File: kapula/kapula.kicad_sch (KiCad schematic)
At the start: 153 parts, among them J1 Conn_02x10_Odd_Even, J12 U.FL, J13 U.FL, J3 Conn_02x10_Odd_Even, J4 Conn_ARM_JTAG_SWD_10, J5 U.FL, J9 U.FL, Q1 AO3401A, Q1 BSS84, Q2 AO3401A, Q3 AO3400A, Q5 AO3400A, Q6 AO3400A, T1 BW21S7511A01TF, T2 BW21S7511A01TF, T3 BW21S7511A01TF, T4 BW21S7511A01TF, U1 XC6206P332MR, U2 TP4054, U3 DW01+G, U5 EFR32FG14P233F256GM48-B, U6 XA213-G4J, X1 DSB221SDN, Y1 32768 Hz

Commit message: PCB: Route TX lowpass again
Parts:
- C24: footprint Capacitor_SMD:C_0402_1005Metric -> kapula:C_0402_to_0603_HandSolder
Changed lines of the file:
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@@
       (effects (font (size 1.27 1.27)))
     )
-    (property "Footprint" "Capacitor_SMD:C_0402_1005Metric" (at 270.51 127.9652 0)
+    (property "Footprint" "kapula:C_0402_to_0603_HandSolder" (at 270.51 127.9652 0)
       (effects (font (size 1.27 1.27)) hide)
     )

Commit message: PCB: Miscellaneous routing
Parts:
- removed TP4: ~, TestPoint:TestPoint_Pad_D1.0mm, symbol Connector:TestPoint
- added C28: 220p, Capacitor_SMD:C_0402_1005Metric, symbol Device:C
- added R22: 0, kapula:R_0402_to_0603_HandSolder, symbol Device:R
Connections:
- net PB12 is gone; now on net SPK_SDN: U5.32 (PB12)
- net GND: now also C28.2
- net SPK_SDN: now also R22.1; no longer U8.1 (SHUTDOWN)
- net VOL_In: now also C28.1
- new net AMP_SDN: R22.2, U8.1 (SHUTDOWN)
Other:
- note added: "TODO: Choose pin for VBAT_ADC (maybe PA4?)"
- note removed: "TODO: Choose pins for SPK_SDN and VBAT_ADC"
- moved on the sheet: C67, C68, C69, C70, C71, FB7, FB8, R39, R40, R41, R42, U8

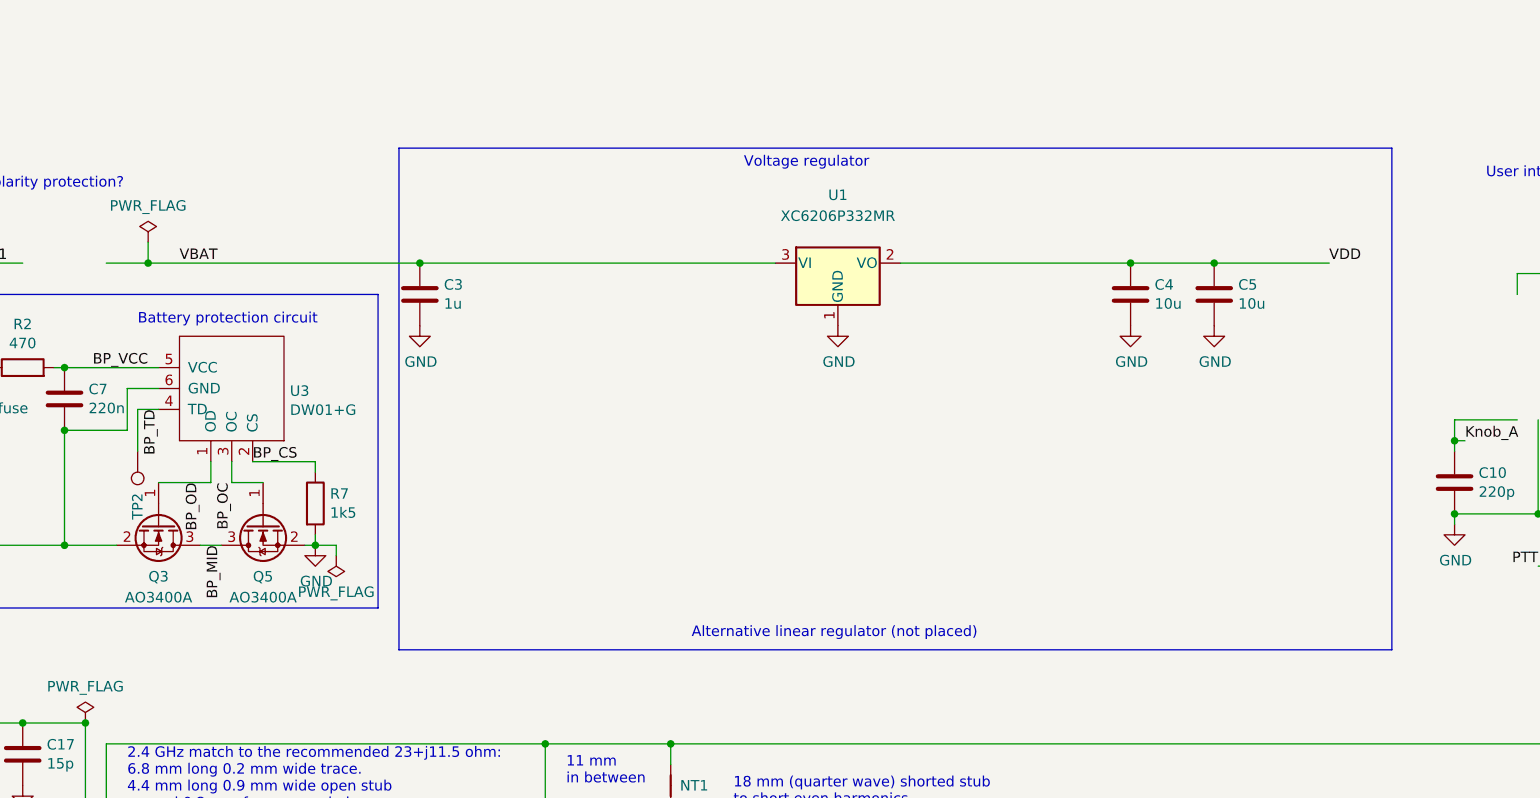
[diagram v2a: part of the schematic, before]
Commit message: PCB: Place and route battery voltage circuits
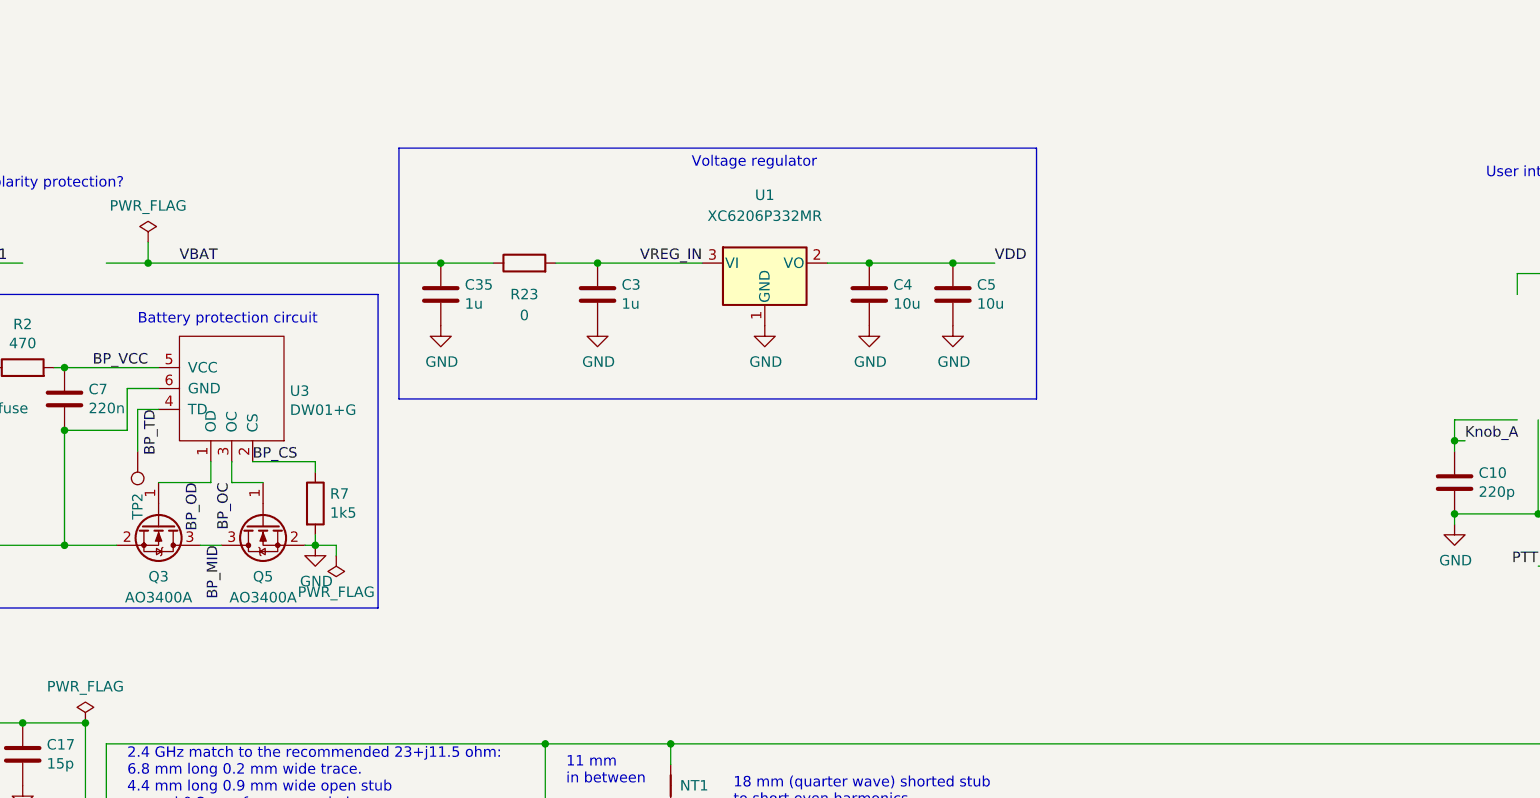
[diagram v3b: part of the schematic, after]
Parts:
- added C35: 1u, Capacitor_SMD:C_0603_1608Metric, symbol Device:C
- added R23: 0, kapula:R_0402_to_0603_HandSolder, symbol Device:R
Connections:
- net GND: now also C35.2
- net VBAT: now also C35.1, R23.1; no longer C3.1, U1.3 (VI)
- new net VREG_IN: C3.1, R23.2, U1.3 (VI)
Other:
- note removed: "Alternative linear regulator (not placed)"
- moved on the sheet: C3, C4, C5, U1

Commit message: PCB: More miscellaneous routing
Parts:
- removed TP3, TP5, TP6: ~, TestPoint:TestPoint_Pad_D1.0mm, symbol Connector:TestPoint
- FB1, FB2: footprint Inductor_SMD:L_0805_2012Metric_Pad1.05x1.20mm_HandSolder -> Inductor_SMD:L_0603_1608Metric_Pad1.05x0.95mm_HandSolder; LCSC TBD -> C1002
- L1: footprint Inductor_SMD:L_Wuerth_MAPI-3010 -> Inductor_SMD:L_1206_3216Metric; LCSC C76865 -> C1049
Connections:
- net GND: now also J6.1 (Pin_1), J6.3 (Pin_3), J6.4 (Pin_4)
- net PA0_TX: now also J3.15 (Pin_15); no longer J6.3 (Pin_3)
- net PA1_RX: now also J3.13 (Pin_13); no longer J6.4 (Pin_4)
- net PA4: now also J3.11 (Pin_11)
- net PA5: now also J3.9 (Pin_9)
- net PB11: now also J3.7 (Pin_7)
- net RESET: no longer J6.1 (Pin_1)
- net RX_EN: now also J3.19 (Pin_19)
- net TX_EN: now also J3.17 (Pin_17)
- net VBAT: now also J3.1 (Pin_1)
- net VDD: now also J3.3 (Pin_3)
- net VDDS: now also J3.5 (Pin_5)
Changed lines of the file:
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@@
   (junction (at 95.25 99.06) (diameter 0) (color 0 0 0 0)
   )
+  (junction (at 334.01 229.87) (diameter 0) (color 0 0 0 0)
+  )
   (junction (at 80.01 255.27) (diameter 0) (color 0 0 0 0)
   )
@@
   (junction (at 69.85 231.14) (diameter 0) (color 0 0 0 0)
   )
+  (junction (at 334.01 232.41) (diameter 0) (color 0 0 0 0)
+  )
   (junction (at 340.36 48.26) (diameter 0) (color 0 0 0 0)
   )
@@
     (stroke (width 0) (type default))
   )
+  (wire (pts (xy 334.01 229.87) (xy 334.01 232.41))
+    (stroke (width 0) (type default))
+  )
   (wire (pts (xy 218.44 177.8) (xy 226.06 177.8))
     (stroke (width 0) (type default))
@@
     (stroke (width 0) (type default))
   )
-  (wire (pts (xy 135.89 93.98) (xy 135.89 101.6))
-    (stroke (width 0) (type default))
-  )
   (wire (pts (xy 173.99 177.8) (xy 185.42 177.8))
     (stroke (width 0) (type default))
@@
     (stroke (width 0) (type default))
   )
-  (wire (pts (xy 140.97 93.98) (xy 140.97 101.6))
-    (stroke (width 0) (type default))
-  )
   (wire (pts (xy 181.61 26.67) (xy 217.17 26.67))
     (stroke (width 0) (type default))
@@
     (stroke (width 0) (type default))
   )
+  (wire (pts (xy 334.01 227.33) (xy 334.01 229.87))
+    (stroke (width 0) (type default))
+  )
   (wire (pts (xy 238.76 233.68) (xy 252.73 233.68))
     (stroke (width 0) (type default))
@@
     (stroke (width 0) (type default))
   )
-  (wire (pts (xy 138.43 101.6) (xy 138.43 93.98))
-    (stroke (width 0) (type default))
-  )
   (wire (pts (xy 307.34 157.48) (xy 307.34 158.75))
     (stroke (width 0) (type default))
@@
     (stroke (width 0) (type default))
   )
+  (wire (pts (xy 334.01 232.41) (xy 334.01 234.95))
+    (stroke (width 0) (type default))
+  )
   (polyline (pts (xy 143.51 215.9) (xy 298.45 215.9))
     (stroke (width 0) (type default))
@@
     (effects (font (size 1.27 1.27)) (justify right bottom))
   )
-  (label "PA1_RX" (at 334.01 234.95 0) (fields_autoplaced)
+  (label "PA1_RX" (at 392.43 182.88 0) (fields_autoplaced)
     (effects (font (size 1.27 1.27)) (justify left bottom))
   )
@@
     (effects (font (size 1.27 1.27)) (justify left bottom))
   )
+  (label "VDDS" (at 392.43 193.04 0) (fields_autoplaced)
+    (effects (font (size 1.27 1.27)) (justify left bottom))
+  )
   (label "VDDS" (at 71.12 180.34 180) (fields_autoplaced)
     (effects (font (size 1.27 1.27)) (justify right bottom))
@@
     (effects (font (size 1.27 1.27)) (justify right bottom))
   )
+  (label "PA4" (at 392.43 185.42 0) (fields_autoplaced)
+    (effects (font (size 1.27 1.27)) (justify left bottom))
+  )
   (label "MIC_EN" (at 80.01 220.98 180) (fields_autoplaced)
     (effects (font (size 1.27 1.27)) (justify right bottom))
@@
     (effects (font (size 1.27 1.27)) (justify left bottom))
   )
+  (label "PA5" (at 392.43 187.96 0) (fields_autoplaced)
+    (effects (font (size 1.27 1.27)) (justify left bottom))
+  )
   (label "SPK-" (at 355.6 190.5 0) (fields_autoplaced)
     (effects (font (size 1.27 1.27)) (justify left bottom))
@@
     (effects (font (size 1.27 1.27)) (justify left bottom))
   )
+  (label "PB11" (at 392.43 190.5 0) (fields_autoplaced)
+    (effects (font (size 1.27 1.27)) (justify left bottom))
+  )
   (label "EFR_VREGSW" (at 110.49 116.84 180) (fields_autoplaced)
     (effects (font (size 1.27 1.27)) (justify right bottom))
@@
     (effects (font (size 1.27 1.27)) (justify right bottom))
   )
+  (label "VDD" (at 392.43 195.58 0) (fields_autoplaced)
+    (effects (font (size 1.27 1.27)) (justify left bottom))
+  )
   (label "VDD" (at 25.4 119.38 180) (fields_autoplaced)
     (effects (font (size 1.27 1.27)) (justify right bottom))
@@
     (effects (font (size 1.27 1.27)) (justify left bottom))
   )
+  (label "VBAT" (at 392.43 198.12 0) (fields_autoplaced)
+    (effects (font (size 1.27 1.27)) (justify left bottom))
+  )
   (label "EFR_DECOUPLE" (at 110.49 124.46 180) (fields_autoplaced)
     (effects (font (size 1.27 1.27)) (justify right bottom))
@@
     (effects (font (size 1.27 1.27)) (justify left bottom))
   )
-  (label "RESET" (at 334.01 227.33 0) (fields_autoplaced)
-    (effects (font (size 1.27 1.27)) (justify left bottom))
-  )
   (label "PA4" (at 140.97 101.6 90) (fields_autoplaced)
     (effects (font (size 1.27 1.27)) (justify left bottom))
@@
     (effects (font (size 1.27 1.27)) (justify left bottom))
   )
+  (label "RX_EN" (at 392.43 175.26 0) (fields_autoplaced)
+    (effects (font (size 1.27 1.27)) (justify left bottom))
+  )
   (label "RX_EN" (at 163.83 114.3 0) (fields_autoplaced)
     (effects (font (size 1.27 1.27)) (justify left bottom))
@@
     (effects (font (size 1.27 1.27)) (justify left bottom))
   )
+  (label "TX_EN" (at 392.43 177.8 0) (fields_autoplaced)
+    (effects (font (size 1.27 1.27)) (justify left bottom))
+  )
   (label "PA1_RX" (at 148.59 101.6 90) (fields_autoplaced)
     (effects (font (size 1.27 1.27)) (justify left bottom))
@@
     (effects (font (size 1.27 1.27)) (justify right bottom))
   )
-  (label "PA0_TX" (at 334.01 232.41 0) (fields_autoplaced)
+  (label "PA0_TX" (at 392.43 180.34 0) (fields_autoplaced)
     (effects (font (size 1.27 1.27)) (justify left bottom))
   )
@@
       (effects (font (size 1.27 1.27)))
     )
-    (property "Footprint" "Inductor_SMD:L_Wuerth_MAPI-3010" (at 87.63 99.06 0)
+    (property "Footprint" "Inductor_SMD:L_1206_3216Metric" (at 87.63 99.06 0)
       (effects (font (size 1.27 1.27)) hide)
     )
-    (property "Datasheet" "https://datasheet.lcsc.com/lcsc/1810261811_TDK-VLS3015ET-4R7M_C76865.pdf" (at 87.63 99.06 0)
+    (property "Datasheet" "https://datasheet.lcsc.com/lcsc/2302231101_FH--Guangdong-Fenghua-Advanced-Tech-CMI321609U4R7KT_C1049.pdf" (at 87.63 99.06 0)
       (effects (font (size 1.27 1.27)) hide)
     )
-    (property "LCSC" "C76865" (at 87.63 99.06 90)
+    (property "LCSC" "C1049" (at 87.63 99.06 90)
       (effects (font (size 1.27 1.27)) hide)
     )
@@
       (effects (font (size 1.27 1.27)))
     )
-    (property "Footprint" "Inductor_SMD:L_0805_2012Metric_Pad1.05x1.20mm_HandSolder" (at 104.14 66.548 90)
+    (property "Footprint" "Inductor_SMD:L_0603_1608Metric_Pad1.05x0.95mm_HandSolder" (at 104.14 66.548 90)
       (effects (font (size 1.27 1.27)) hide)
     )
@@
       (effects (font (size 1.27 1.27)) hide)
     )
-    (property "LCSC" "TBD" (at 104.14 64.77 0)
+    (property "LCSC" "C1002" (at 104.14 64.77 0)
       (effects (font (size 1.27 1.27)) hide)
     )
@@
       (effects (font (size 1.27 1.27)))
     )
-    (property "Footprint" "Inductor_SMD:L_0805_2012Metric_Pad1.05x1.20mm_HandSolder" (at 114.3 170.688 90)
+    (property "Footprint" "Inductor_SMD:L_0603_1608Metric_Pad1.05x0.95mm_HandSolder" (at 114.3 170.688 90)
       (effects (font (size 1.27 1.27)) hide)
     )
@@
       (effects (font (size 1.27 1.27)) hide)
     )
-    (property "LCSC" "TBD" (at 114.3 168.91 0)
+    (property "LCSC" "C1002" (at 114.3 168.91 0)
       (effects (font (size 1.27 1.27)) hide)
     )
@@
     )
   )
-  (symbol (lib_id "Connector:TestPoint") (at 138.43 93.98 0) (unit 1)
-    (in_bom yes) (on_board yes) (dnp no)
-    (property "Reference" "TP6" (at 138.43 88.9 90)
-      (effects (font (size 1.27 1.27)) (justify left))
-    )
-    (property "Value" "~" (at 136.9568 91.0082 0)
-      (effects (font (size 1.27 1.27)) (justify right))
-    )
-    (property "Footprint" "TestPoint:TestPoint_Pad_D1.0mm" (at 143.51 93.98 0)
-      (effects (font (size 1.27 1.27)) hide)
-    )
-    (property "Datasheet" "" (at 143.51 93.98 0)
-      (effects (font (size 1.27 1.27)) hide)
-    )
-    (pin "1")
-    (instances
-      (project "kapula"
-        (path "/f2315993-072e-45c9-8c85-e79c6d40aba4"
-          (reference "TP6") (unit 1)
-        )
-      )
-    )
-  )
-  (symbol (lib_id "Connector:TestPoint") (at 135.89 93.98 0) (unit 1)
-    (in_bom yes) (on_board yes) (dnp no)
-    (property "Reference" "TP5" (at 135.89 88.9 90)
-      (effects (font (size 1.27 1.27)) (justify left))
-    )
-    (property "Value" "~" (at 134.4168 91.0082 0)
-      (effects (font (size 1.27 1.27)) (justify right))
-    )
-    (property "Footprint" "TestPoint:TestPoint_Pad_D1.0mm" (at 140.97 93.98 0)
-      (effects (font (size 1.27 1.27)) hide)
-    )
-    (property "Datasheet" "" (at 140.97 93.98 0)
-      (effects (font (size 1.27 1.27)) hide)
-    )
-    (pin "1")
-    (instances
-      (project "kapula"
-        (path "/f2315993-072e-45c9-8c85-e79c6d40aba4"
-          (reference "TP5") (unit 1)
-        )
-      )
-    )
-  )
   (symbol (lib_id "Connector_Generic:Conn_01x04") (at 328.93 229.87 0) (mirror y) (unit 1)
     (in_bom yes) (on_board yes) (dnp no)
@@
         )
       )
-    )
-  )
-  (symbol (lib_id "Connector:TestPoint") (at 140.97 93.98 0) (unit 1)
-    (in_bom yes) (on_board yes) (dnp no)
-    (property "Reference" "TP3" (at 140.97 88.9 90)
-      (effects (font (size 1.27 1.27)) (justify left))
-    )
-    (property "Value" "~" (at 139.4968 91.0082 0)
-      (effects (font (size 1.27 1.27)) (justify right))
-    )
-    (property "Footprint" "TestPoint:TestPoint_Pad_D1.0mm" (at 146.05 93.98 0)
-      (effects (font (size 1.27 1.27)) hide)
-    )
-    (property "Datasheet" "" (at 146.05 93.98 0)
-      (effects (font (size 1.27 1.27)) hide)
-    )
-    (pin "1")
-    (instances
-      (project "kapula"
-        (path "/f2315993-072e-45c9-8c85-e79c6d40aba4"
-          (reference "TP3") (unit 1)
-        )
-      )

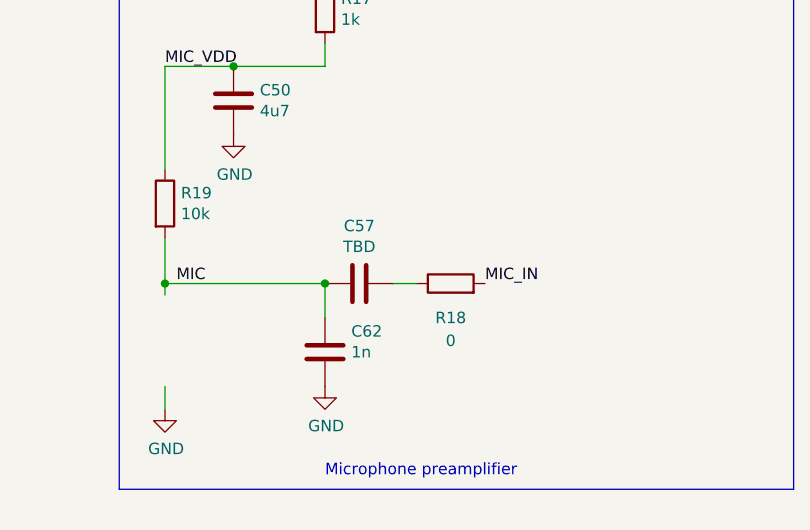
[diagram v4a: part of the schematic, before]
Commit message: PCB: Route more power supply lines
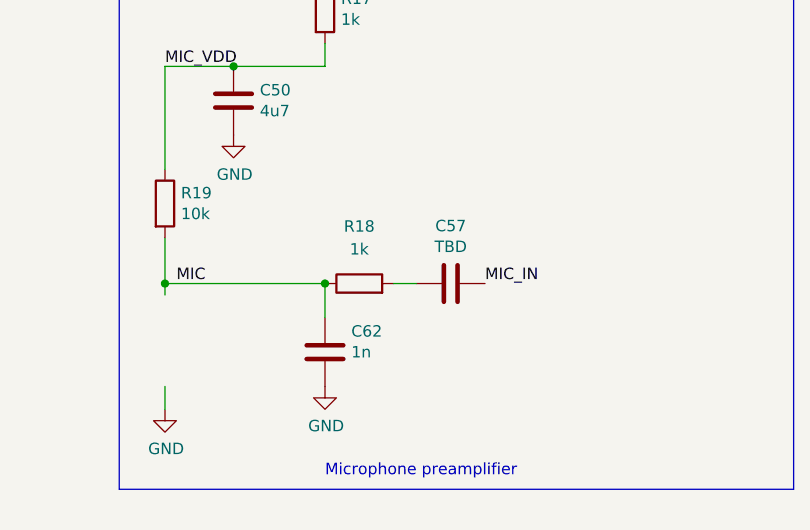
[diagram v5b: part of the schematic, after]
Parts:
- R18: value 0 -> 1k; LCSC C17168 -> C11702
- R4: footprint kapula:R_0402_to_0603_HandSolder -> Resistor_SMD:R_0402_1005Metric
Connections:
- net MIC: now also R18.1; no longer C57.2
- net MIC_IN: now also C57.1; no longer R18.2
- new net: C57.2, R18.2
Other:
- moved on the sheet: C57, R18
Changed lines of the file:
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@@
   (junction (at 439.42 252.73) (diameter 0) (color 0 0 0 0)
   )
+  (junction (at 80.01 255.27) (diameter 0) (color 0 0 0 0)
+  )
   (junction (at 173.99 82.55) (diameter 0) (color 0 0 0 0)
   )
@@
   (junction (at 334.01 229.87) (diameter 0) (color 0 0 0 0)
   )
-  (junction (at 80.01 255.27) (diameter 0) (color 0 0 0 0)
-  )
   (junction (at 185.42 127) (diameter 0) (color 0 0 0 0)
   )
@@
     )
   )
-  (symbol (lib_id "Device:C") (at 83.82 255.27 270) (unit 1)
+  (symbol (lib_id "Device:C") (at 93.98 255.27 270) (unit 1)
     (in_bom yes) (on_board yes) (dnp no)
-    (property "Reference" "C57" (at 83.82 248.8692 90)
+    (property "Reference" "C57" (at 93.98 248.8692 90)
       (effects (font (size 1.27 1.27)))
     )
-    (property "Value" "TBD" (at 83.82 251.1806 90)
+    (property "Value" "TBD" (at 93.98 251.1806 90)
       (effects (font (size 1.27 1.27)))
     )
-    (property "Footprint" "Capacitor_SMD:C_0402_1005Metric" (at 80.01 256.2352 0)
+    (property "Footprint" "Capacitor_SMD:C_0402_1005Metric" (at 90.17 256.2352 0)
       (effects (font (size 1.27 1.27)) hide)
     )
-    (property "Datasheet" "" (at 83.82 255.27 0)
+    (property "Datasheet" "" (at 93.98 255.27 0)
       (effects (font (size 1.27 1.27)) hide)
     )
-    (property "LCSC" "" (at 83.82 255.27 0)
+    (property "LCSC" "" (at 93.98 255.27 0)
       (effects (font (size 1.27 1.27)) hide)
     )
@@
       (effects (font (size 1.27 1.27)))
     )
-    (property "Footprint" "kapula:R_0402_to_0603_HandSolder" (at 386.08 43.688 90)
+    (property "Footprint" "Resistor_SMD:R_0402_1005Metric" (at 386.08 43.688 90)
       (effects (font (size 1.27 1.27)) hide)
     )
@@
     )
   )
-  (symbol (lib_id "Device:R") (at 93.98 255.27 90) (unit 1)
+  (symbol (lib_id "Device:R") (at 83.82 255.27 90) (unit 1)
     (in_bom yes) (on_board yes) (dnp no) (fields_autoplaced)
-    (property "Reference" "R18" (at 93.98 259.08 90)
+    (property "Reference" "R18" (at 83.82 248.92 90)
       (effects (font (size 1.27 1.27)))
     )
-    (property "Value" "0" (at 93.98 261.62 90)
+    (property "Value" "1k" (at 83.82 251.46 90)
       (effects (font (size 1.27 1.27)))
     )
-    (property "Footprint" "Resistor_SMD:R_0402_1005Metric" (at 93.98 257.048 90)
+    (property "Footprint" "Resistor_SMD:R_0402_1005Metric" (at 83.82 257.048 90)
       (effects (font (size 1.27 1.27)) hide)
     )
-    (property "Datasheet" "" (at 93.98 255.27 0)
+    (property "Datasheet" "" (at 83.82 255.27 0)
       (effects (font (size 1.27 1.27)) hide)
     )
-    (property "LCSC" "C17168" (at 93.98 255.27 0)
+    (property "LCSC" "C11702" (at 83.82 255.27 0)
       (effects (font (size 1.27 1.27)) hide)
     )
